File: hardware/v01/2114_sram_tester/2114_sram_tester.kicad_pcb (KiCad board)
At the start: 2 copper layers, 67.3 x 62.2 mm, 7 parts, among them J1 Conn_02x09_Counter_Clockwise

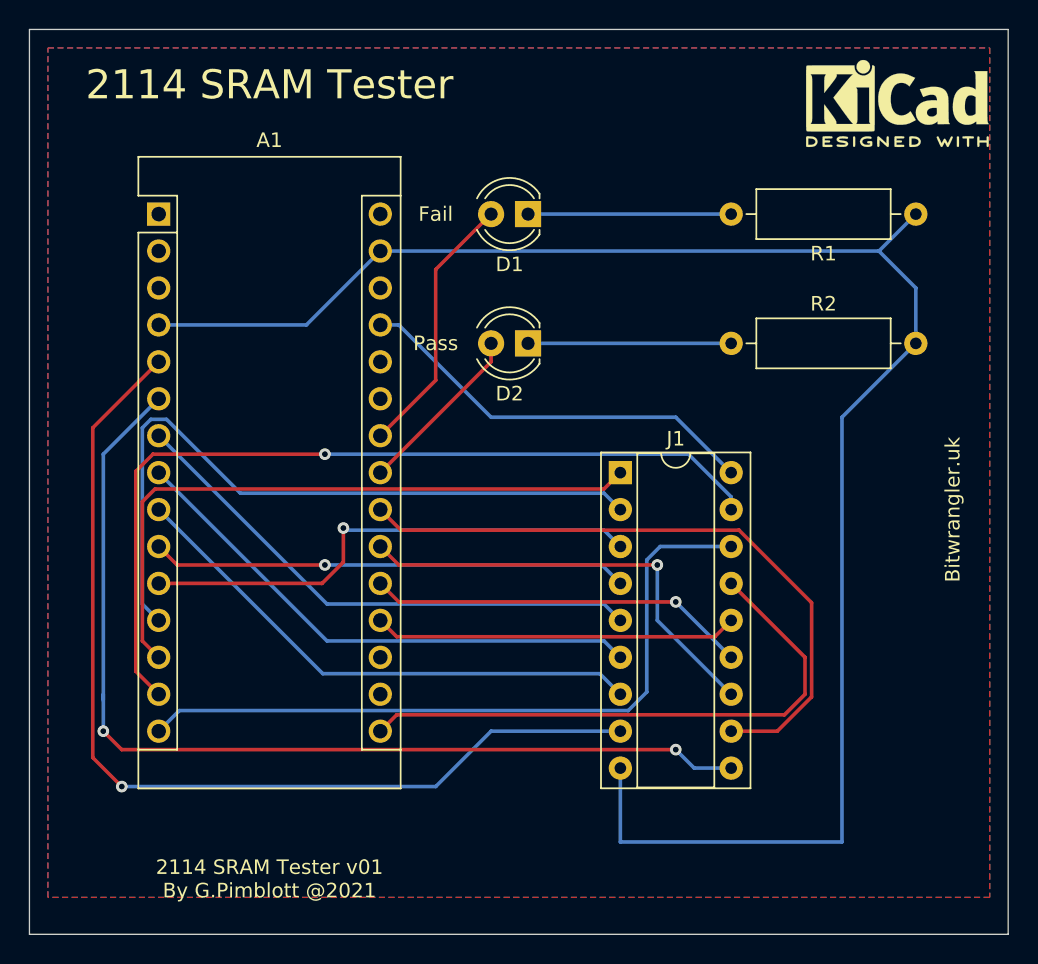
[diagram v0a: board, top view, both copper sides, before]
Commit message: Updated hardware
Updated hardware to include stop/start button
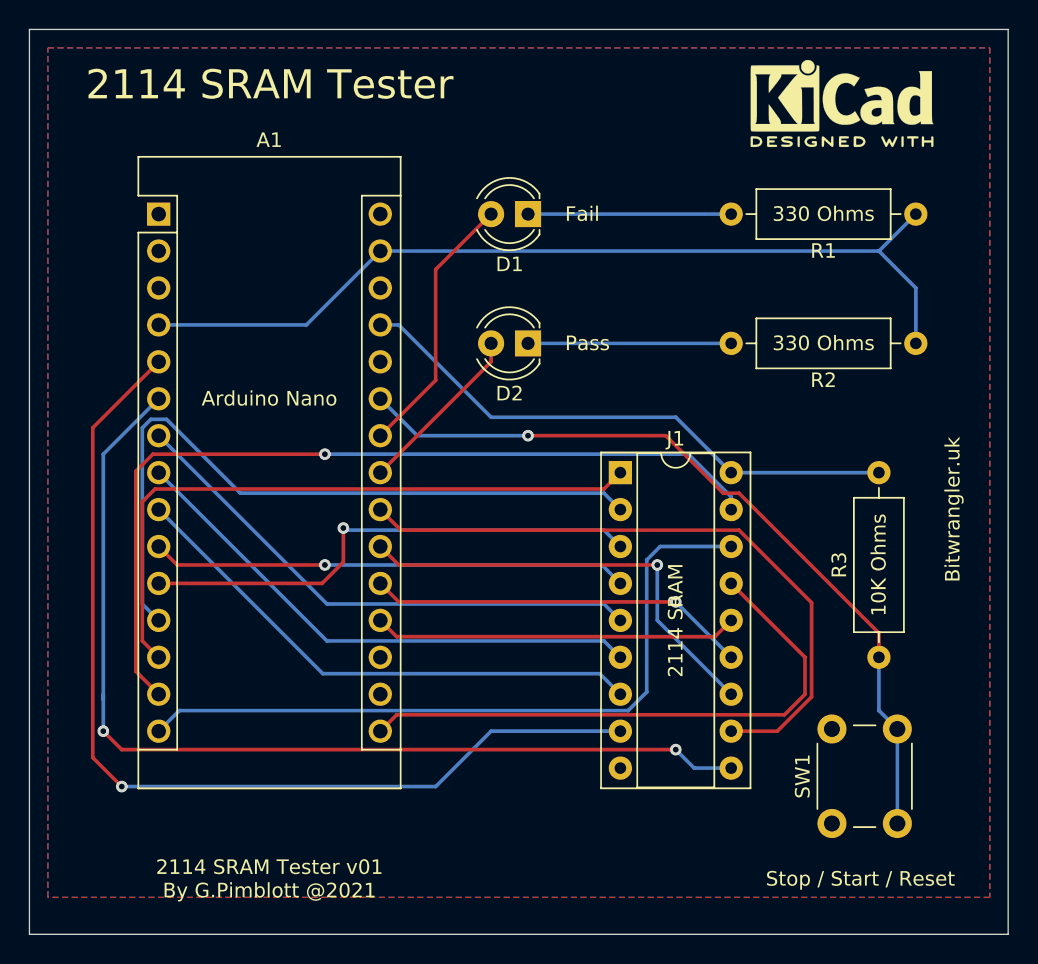
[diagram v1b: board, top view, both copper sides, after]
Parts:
- added R3: 10K Ohms, Resistor_THT:R_Axial_DIN0309_L9.0mm_D3.2mm_P12.70mm_Horizontal, F.Cu at (148.6, 92.7)
- added SW1: SW_Push, Button_Switch_THT:SW_PUSH_6mm, F.Cu at (145.4, 104.1)
- moved REF** 3.81 mm to (146.1, 54.6)
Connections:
- A1 pad 25: Net-(A1-Pad25) -> Switch
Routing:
- net GND: track 119.3 -> 62.6 mm
- net Switch: track 0.00 -> 54.6 mm, vias 0 -> 1
- net 5vPower: track 28.3 -> 38.5 mm
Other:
- board text added: "10K Ohms"
- board text added: "2114 SRAM"
- board text added: "330 Ohms"
- board text added: "Arduino Nano"
- board text added: "Stop / Start / Reset"
